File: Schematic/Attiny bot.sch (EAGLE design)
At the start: 25 parts, among them IC1 L293D

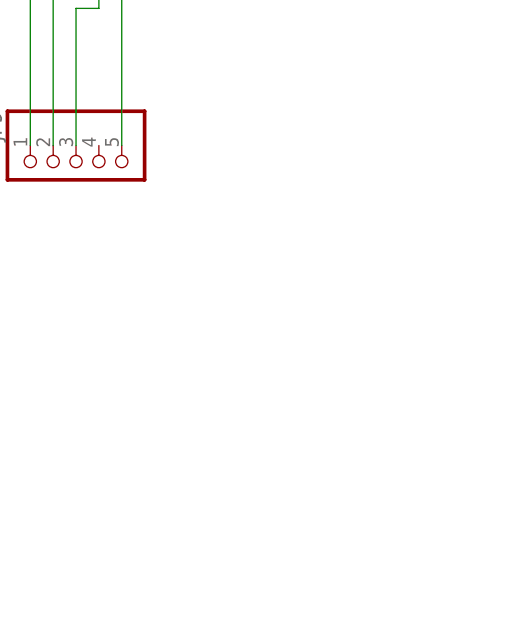
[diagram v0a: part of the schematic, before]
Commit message: Schematic of Cing
Adding Ambient sensor
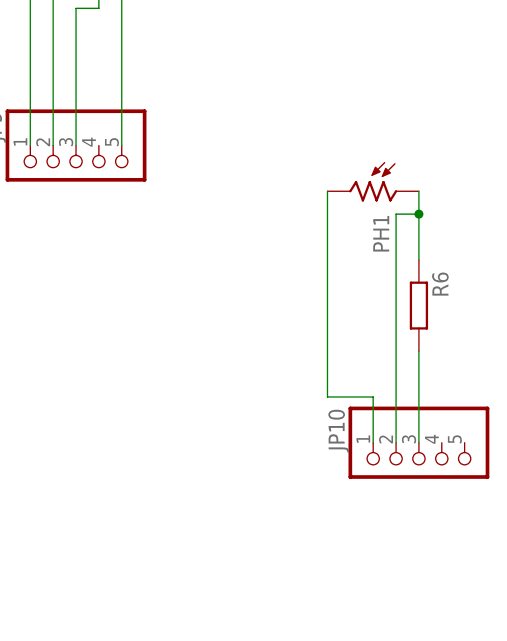
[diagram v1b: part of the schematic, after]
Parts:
- added JP10: (no value), pinhead:PINHD-1X5
- added PH1: B1060_23, photo-elements:B1060_23
- added R6: (no value), rcl:R-EU_R1206
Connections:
- new net N$13: JP10.2, PH1.1, R6.1
- new net N$14: JP10.3, R6.2
- new net N$15: JP10.1, PH1.2
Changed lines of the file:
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@@
 <part name="U$3" library="diy-modules" deviceset="ULTRASONIC-HC-SR04" device="#V"/>
 <part name="JP9" library="pinhead" deviceset="PINHD-1X5" device=""/>
+<part name="JP10" library="pinhead" deviceset="PINHD-1X5" device=""/>
+<part name="PH1" library="photo-elements" deviceset="?1060*" device="B" technology="_23" value=""/>
+<part name="R6" library="rcl" deviceset="R-EU_" device="R1206"/>
 </parts>
 <sheets>
@@
 <instance part="U$3" gate="G$1" x="276.86" y="198.12"/>
 <instance part="JP9" gate="A" x="279.4" y="154.94" rot="MR270"/>
+<instance part="JP10" gate="A" x="317.5" y="121.92" rot="MR270"/>
+<instance part="PH1" gate="G$1" x="312.42" y="152.4" rot="R270"/>
+<instance part="R6" gate="G$1" x="317.5" y="139.7" rot="R270"/>
 </instances>
 <busses>
@@
 </segment>
 </net>
+<net name="N$13" class="0">
+<segment>
+<pinref part="PH1" gate="G$1" pin="1"/>
+<pinref part="R6" gate="G$1" pin="1"/>
+<wire x1="317.5" y1="144.78" x2="317.5" y2="149.86" width="0.1524" layer="91"/>
+<pinref part="JP10" gate="A" pin="2"/>
+<wire x1="317.5" y1="149.86" x2="317.5" y2="152.4" width="0.1524" layer="91"/>
+<wire x1="314.96" y1="124.46" x2="314.96" y2="149.86" width="0.1524" layer="91"/>
+<wire x1="314.96" y1="149.86" x2="317.5" y2="149.86" width="0.1524" layer="91"/>
+<junction x="317.5" y="149.86"/>
+</segment>
+</net>
+<net name="N$14" class="0">
+<segment>
+<pinref part="JP10" gate="A" pin="3"/>
+<pinref part="R6" gate="G$1" pin="2"/>
+<wire x1="317.5" y1="134.62" x2="317.5" y2="124.46" width="0.1524" layer="91"/>
+</segment>
+</net>
+<net name="N$15" class="0">
+<segment>
+<pinref part="PH1" gate="G$1" pin="2"/>
+<wire x1="307.34" y1="152.4" x2="307.34" y2="129.54" width="0.1524" layer="91"/>
+<wire x1="307.34" y1="129.54" x2="312.42" y2="129.54" width="0.1524" layer="91"/>
+<pinref part="JP10" gate="A" pin="1"/>
+<wire x1="312.42" y1="129.54" x2="312.42" y2="124.46" width="0.1524" layer="91"/>
+</segment>
+</net>
